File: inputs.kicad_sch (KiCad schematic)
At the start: 31 parts, among them J3 MAP_Connector, U3 SP720

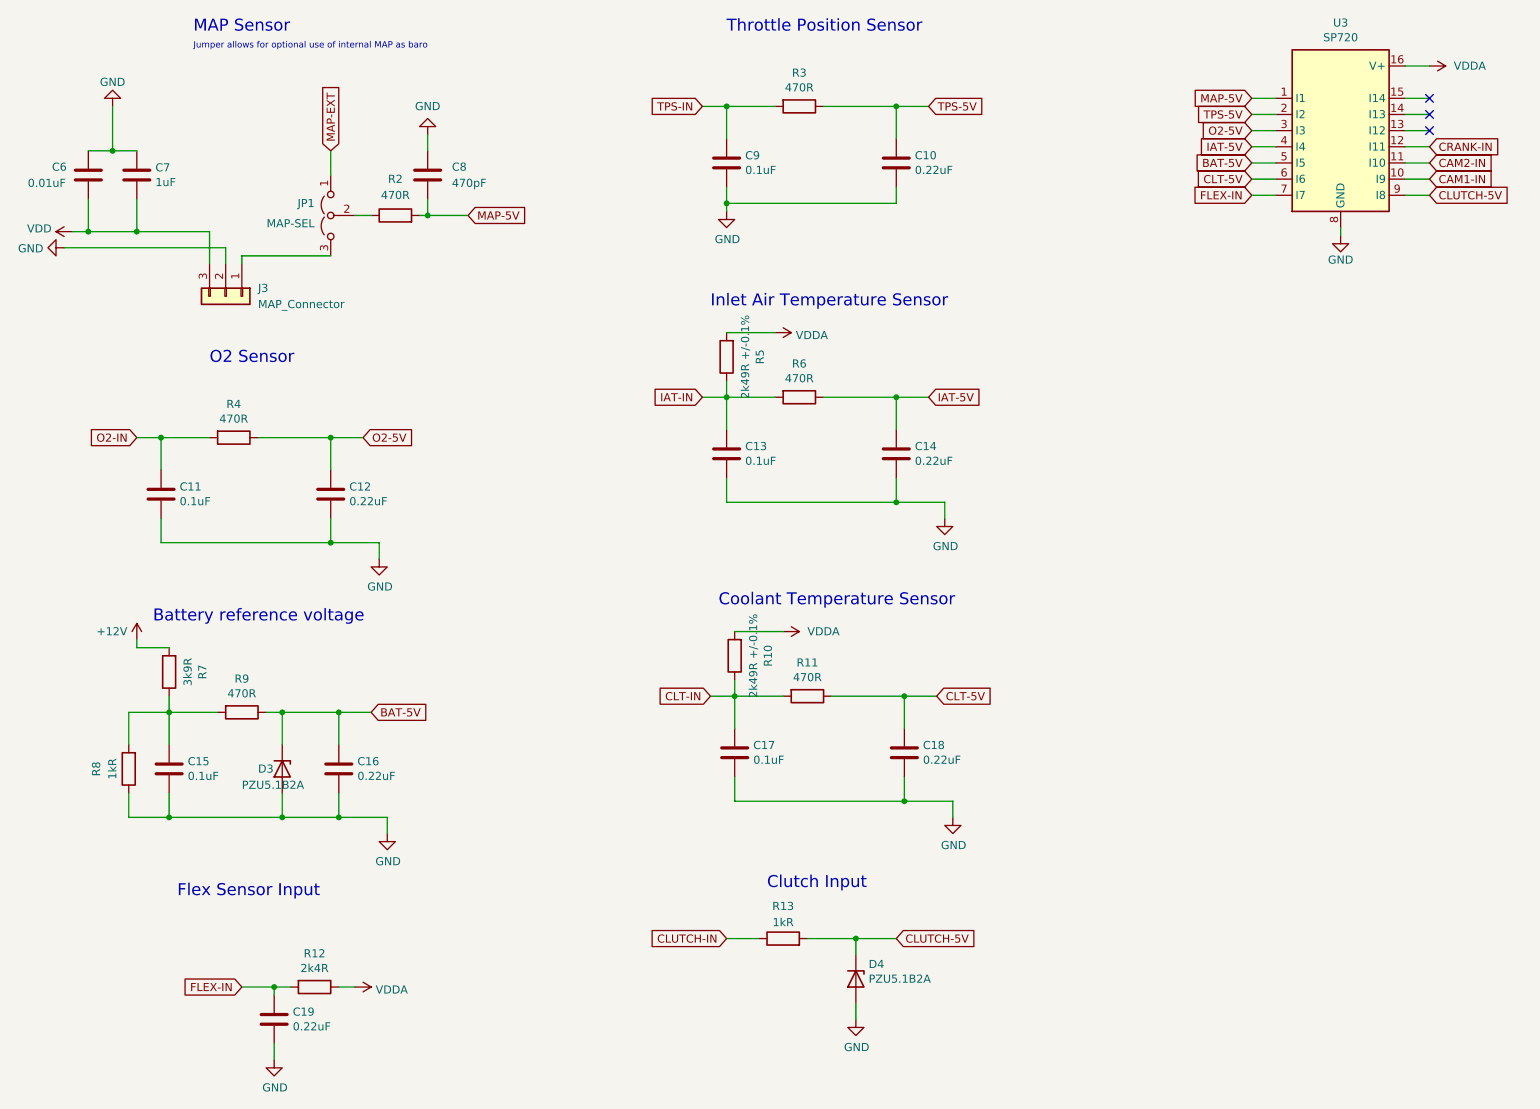
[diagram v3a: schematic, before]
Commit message: Completed layout, slight changes to schematic to optimise routing, 12V proto supply rail removed
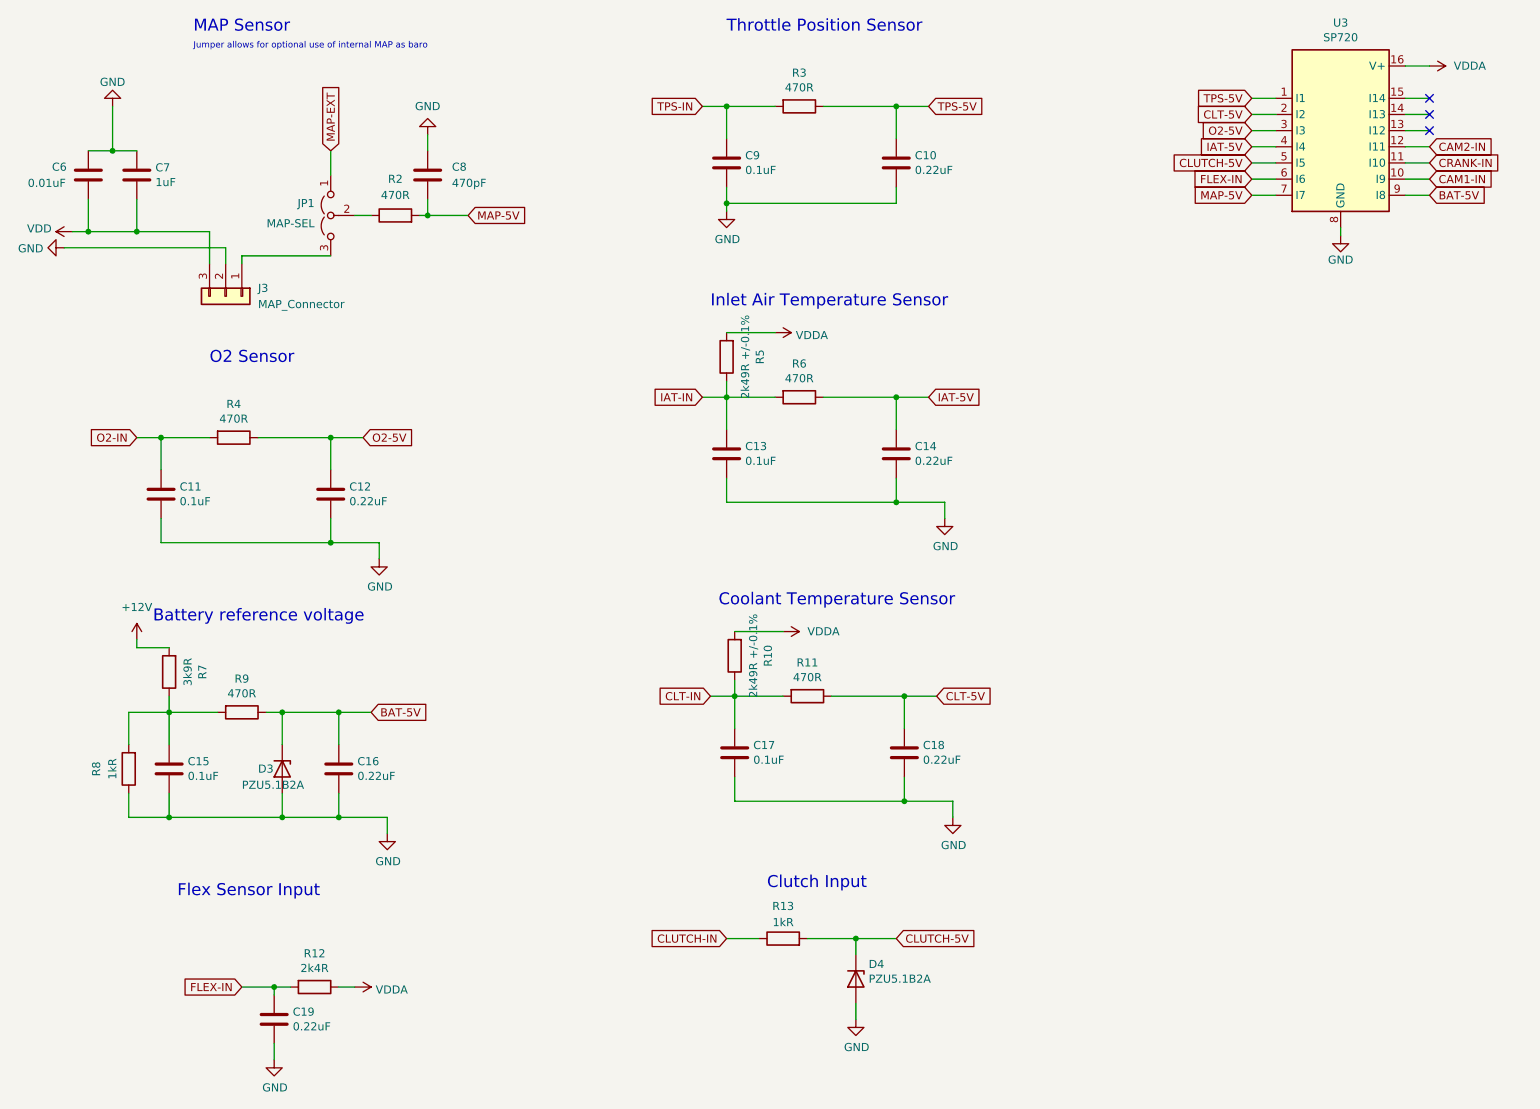
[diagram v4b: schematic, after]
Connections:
- net BAT-5V: now also U3.9 (I8); no longer U3.5 (I5)
- net CAM2-IN: now also U3.12 (I11); no longer U3.11 (I10)
- net CLT-5V: now also U3.2 (I2); no longer U3.6 (I6)
- net CLUTCH-5V: now also U3.5 (I5); no longer U3.9 (I8)
- net CRANK-IN: now also U3.11 (I10); no longer U3.12 (I11)
- net FLEX-IN: now also U3.6 (I6); no longer U3.7 (I7)
- net MAP-5V: now also U3.7 (I7); no longer U3.1 (I1)
- net TPS-5V: now also U3.1 (I1); no longer U3.2 (I2)
- net VDD: no longer R7.2, U3.16 (V+)
- net VDDA: now also U3.16 (V+)
- new net +12V: R7.2
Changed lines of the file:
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@@
     )
   )
-  (global_label "TPS-5V" (shape input) (at 212.09 34.29 180) (fields_autoplaced)
+  (global_label "TPS-5V" (shape input) (at 212.09 31.75 180) (fields_autoplaced)
     (effects (font (size 1.27 1.27)) (justify right))
-    (property "Intersheet References" "${INTERSHEET_REFS}" (id 0) (at 202.3593 34.2106 0)
+    (property "Intersheet References" "${INTERSHEET_REFS}" (id 0) (at 202.3593 31.6706 0)
       (effects (font (size 1.27 1.27)) (justify right) hide)
     )
   )
-  (global_label "FLEX-IN" (shape input) (at 212.09 46.99 180) (fields_autoplaced)
+  (global_label "FLEX-IN" (shape input) (at 212.09 44.45 180) (fields_autoplaced)
     (effects (font (size 1.27 1.27)) (justify right))
-    (property "Intersheet References" "${INTERSHEET_REFS}" (id 0) (at 201.694 46.9106 0)
+    (property "Intersheet References" "${INTERSHEET_REFS}" (id 0) (at 201.694 44.3706 0)
       (effects (font (size 1.27 1.27)) (justify right) hide)
     )
@@
     )
   )
-  (global_label "CAM2-IN" (shape input) (at 240.03 41.91 0) (fields_autoplaced)
+  (global_label "CAM2-IN" (shape input) (at 240.03 39.37 0) (fields_autoplaced)
     (effects (font (size 1.27 1.27)) (justify left))
-    (property "Intersheet References" "${INTERSHEET_REFS}" (id 0) (at 250.9702 41.8306 0)
+    (property "Intersheet References" "${INTERSHEET_REFS}" (id 0) (at 250.9702 39.2906 0)
       (effects (font (size 1.27 1.27)) (justify left) hide)
     )
@@
     )
   )
-  (global_label "MAP-5V" (shape input) (at 212.09 31.75 180) (fields_autoplaced)
+  (global_label "MAP-5V" (shape input) (at 212.09 46.99 180) (fields_autoplaced)
     (effects (font (size 1.27 1.27)) (justify right))
-    (property "Intersheet References" "${INTERSHEET_REFS}" (id 0) (at 201.9964 31.6706 0)
+    (property "Intersheet References" "${INTERSHEET_REFS}" (id 0) (at 201.9964 46.9106 0)
       (effects (font (size 1.27 1.27)) (justify right) hide)
     )
@@
     )
   )
-  (global_label "CRANK-IN" (shape input) (at 240.03 39.37 0) (fields_autoplaced)
+  (global_label "CRANK-IN" (shape input) (at 240.03 41.91 0) (fields_autoplaced)
     (effects (font (size 1.27 1.27)) (justify left))
-    (property "Intersheet References" "${INTERSHEET_REFS}" (id 0) (at 252.1798 39.2906 0)
+    (property "Intersheet References" "${INTERSHEET_REFS}" (id 0) (at 252.1798 41.8306 0)
       (effects (font (size 1.27 1.27)) (justify left) hide)
     )
@@
     )
   )
-  (global_label "CLT-5V" (shape input) (at 212.09 44.45 180) (fields_autoplaced)
+  (global_label "CLT-5V" (shape input) (at 212.09 34.29 180) (fields_autoplaced)
     (effects (font (size 1.27 1.27)) (justify right))
-    (property "Intersheet References" "${INTERSHEET_REFS}" (id 0) (at 202.5407 44.3706 0)
+    (property "Intersheet References" "${INTERSHEET_REFS}" (id 0) (at 202.5407 34.2106 0)
       (effects (font (size 1.27 1.27)) (justify right) hide)
     )
@@
     )
   )
-  (global_label "BAT-5V" (shape input) (at 212.09 41.91 180) (fields_autoplaced)
-    (effects (font (size 1.27 1.27)) (justify right))
-    (property "Intersheet References" "${INTERSHEET_REFS}" (id 0) (at 202.4802 41.8306 0)
-      (effects (font (size 1.27 1.27)) (justify right) hide)
+  (global_label "BAT-5V" (shape input) (at 240.03 46.99 0) (fields_autoplaced)
+    (effects (font (size 1.27 1.27)) (justify left))
+    (property "Intersheet References" "${INTERSHEET_REFS}" (id 0) (at 249.6398 47.0694 0)
+      (effects (font (size 1.27 1.27)) (justify left) hide)
     )
   )
@@
     )
   )
-  (global_label "CLUTCH-5V" (shape input) (at 240.03 46.99 0) (fields_autoplaced)
-    (effects (font (size 1.27 1.27)) (justify left))
-    (property "Intersheet References" "${INTERSHEET_REFS}" (id 0) (at 253.5102 46.9106 0)
-      (effects (font (size 1.27 1.27)) (justify left) hide)
+  (global_label "CLUTCH-5V" (shape input) (at 212.09 41.91 180) (fields_autoplaced)
+    (effects (font (size 1.27 1.27)) (justify right))
+    (property "Intersheet References" "${INTERSHEET_REFS}" (id 0) (at 198.6098 41.9894 0)
+      (effects (font (size 1.27 1.27)) (justify right) hide)
     )
   )
@@
     (pin "2")
   )
+  (symbol (lib_id "power:+12V") (at 36.83 116.84 0) (unit 1)
+    (in_bom yes) (on_board yes) (fields_autoplaced)
+    (property "Reference" "#PWR0152" (id 0) (at 36.83 120.65 0)
+      (effects (font (size 1.27 1.27)) hide)
+    )
+    (property "Value" "+12V" (id 1) (at 36.83 111.76 0))
+    (property "Footprint" "" (id 2) (at 36.83 116.84 0)
+      (effects (font (size 1.27 1.27)) hide)
+    )
+    (property "Datasheet" "" (id 3) (at 36.83 116.84 0)
+      (effects (font (size 1.27 1.27)) hide)
+    )
+    (pin "1")
+  )
   (symbol (lib_id "power:GND") (at 33.02 33.02 180) (unit 1)
     (in_bom yes) (on_board yes)
@@
     )
     (property "Datasheet" "" (id 3) (at 226.06 53.34 0)
+      (effects (font (size 1.27 1.27)) hide)
+    )
+    (pin "1")
+  )
+  (symbol (lib_id "power:VDDA") (at 240.03 26.67 270) (unit 1)
+    (in_bom yes) (on_board yes) (fields_autoplaced)
+    (property "Reference" "#PWR0153" (id 0) (at 236.22 26.67 0)
+      (effects (font (size 1.27 1.27)) hide)
+    )
+    (property "Value" "VDDA" (id 1) (at 243.84 26.6699 90)
+      (effects (font (size 1.27 1.27)) (justify left))
+    )
+    (property "Footprint" "" (id 2) (at 240.03 26.67 0)
+      (effects (font (size 1.27 1.27)) hide)
+    )
+    (property "Datasheet" "" (id 3) (at 240.03 26.67 0)
       (effects (font (size 1.27 1.27)) hide)
     )
@@
     (pin "3")
   )
-  (symbol (lib_id "power:VDD") (at 240.03 26.67 270) (unit 1)
-    (in_bom yes) (on_board yes) (fields_autoplaced)
-    (property "Reference" "#PWR0153" (id 0) (at 236.22 26.67 0)
-      (effects (font (size 1.27 1.27)) hide)
-    )
-    (property "Value" "VDDA" (id 1) (at 243.84 26.6699 90)
-      (effects (font (size 1.27 1.27)) (justify left))
-    )
-    (property "Footprint" "" (id 2) (at 240.03 26.67 0)
-      (effects (font (size 1.27 1.27)) hide)
-    )
-    (property "Datasheet" "" (id 3) (at 240.03 26.67 0)
-      (effects (font (size 1.27 1.27)) hide)
-    )
-    (pin "1")
-  )
   (symbol (lib_id "Connector_Generic:Conn_01x03") (at 50.8 62.865 270) (unit 1)
     (in_bom yes) (on_board yes) (fields_autoplaced)
@@
     (pin "2")
   )
-  (symbol (lib_id "power:VDD") (at 36.83 116.84 0) (unit 1)
-    (in_bom yes) (on_board yes)
-    (property "Reference" "#PWR0152" (id 0) (at 36.83 120.65 0)
-      (effects (font (size 1.27 1.27)) hide)
-    )
-    (property "Value" "+12V" (id 1) (at 30.48 115.57 0)
-      (effects (font (size 1.27 1.27)) (justify left))
-    )
-    (property "Footprint" "" (id 2) (at 36.83 116.84 0)
-      (effects (font (size 1.27 1.27)) hide)
-    )
-    (property "Datasheet" "" (id 3) (at 36.83 116.84 0)
-      (effects (font (size 1.27 1.27)) hide)
-    )
-    (pin "1")
-  )
 )
